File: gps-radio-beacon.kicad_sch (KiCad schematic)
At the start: 52 parts, among them J1 Conn_Coaxial, J2 Conn_01x16, J3 Conn_Coaxial, J4 Conn_01x16, J5 Conn_01x02, P1 USB_C_Plug_USB2.0, Q1 Q_PMOS_DGS, SW1 SW_Push, U1 RP2040, U2 MAX-M8Q, U3 W25Q128JVS, U4 NCP1117-3.3_SOT223, Y1 Crystal

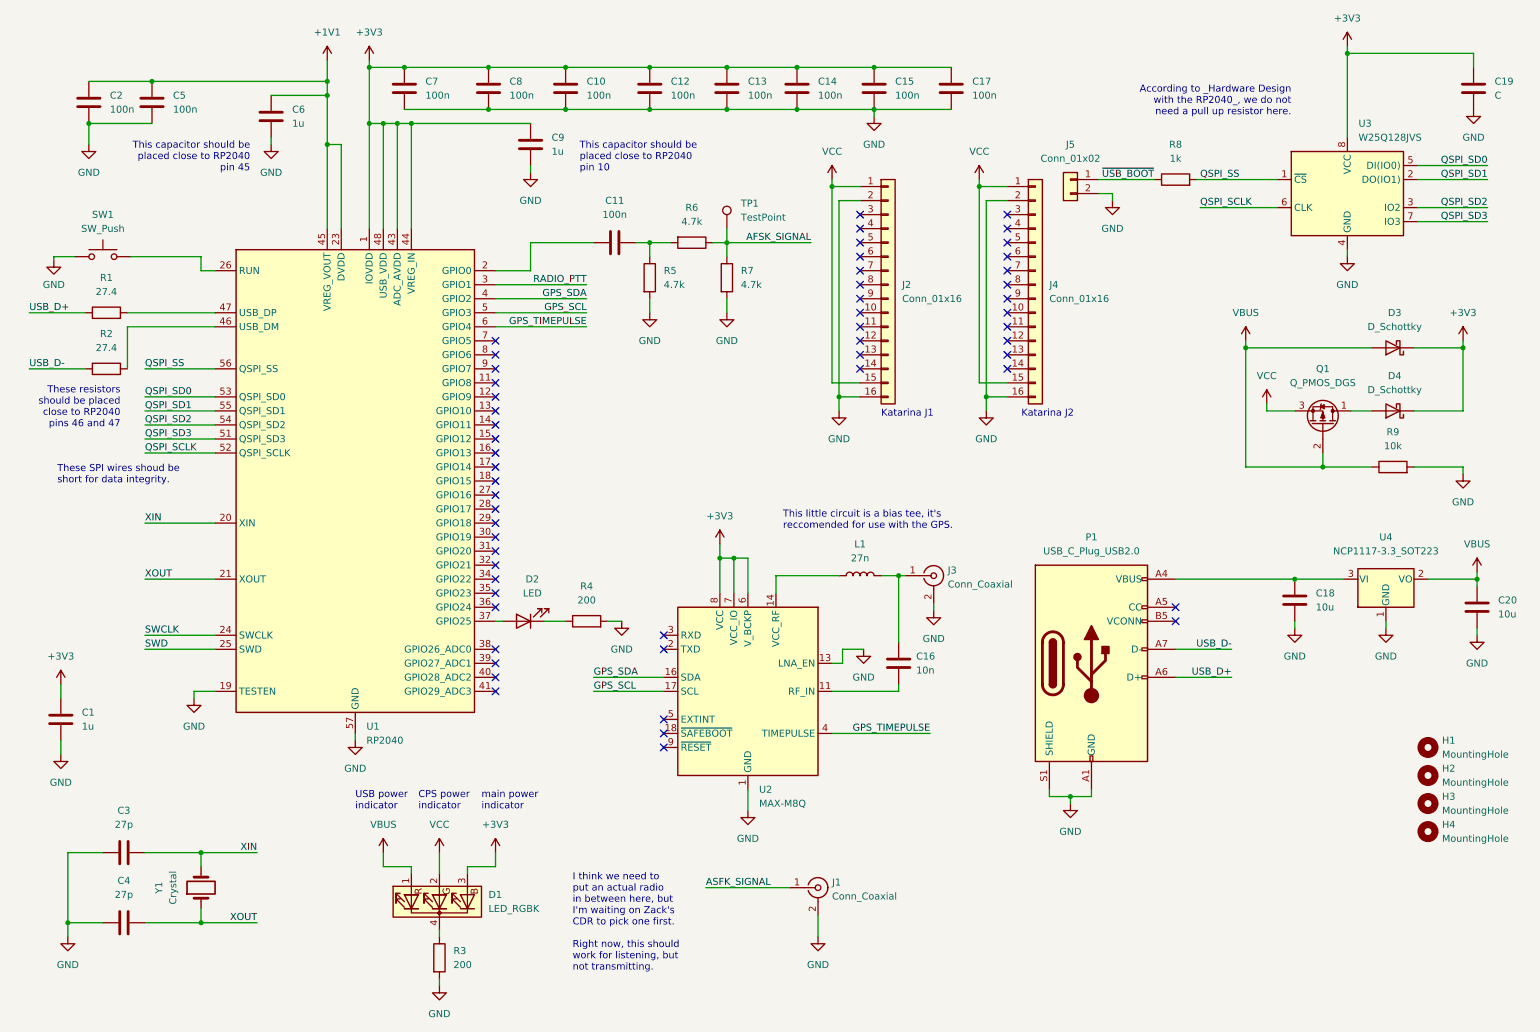
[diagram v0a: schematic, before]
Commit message: fix ERC violations
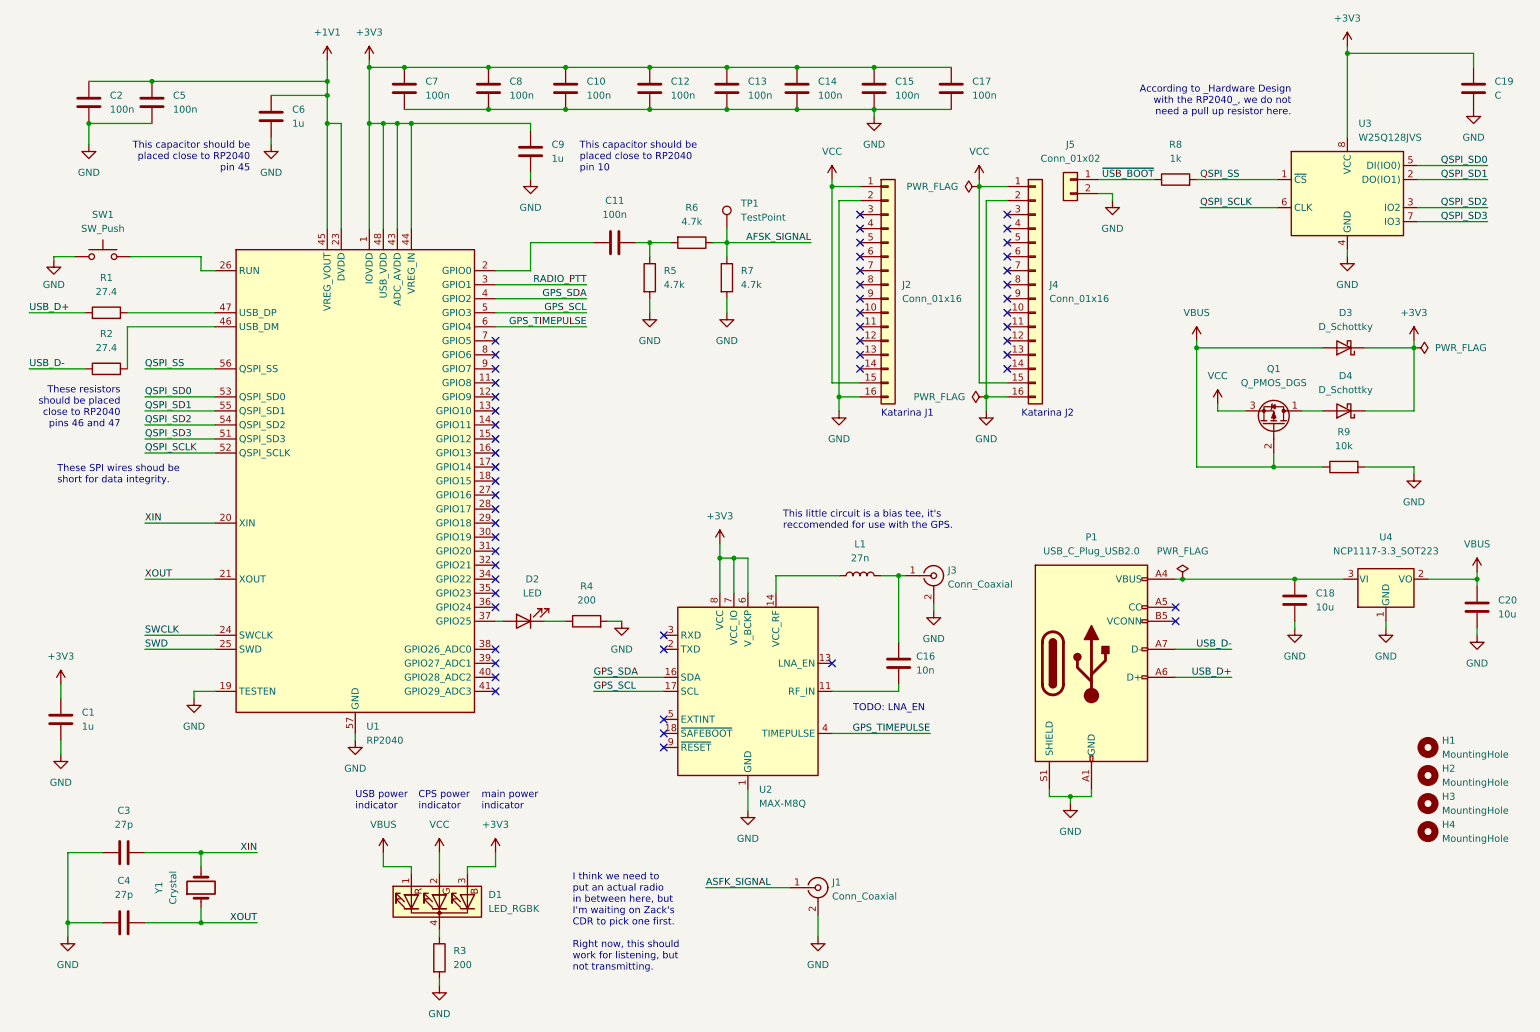
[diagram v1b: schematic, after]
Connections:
- net GND: no longer U2.13 (LNA_EN)
- no-connect marks 55 -> 56
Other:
- note added: "TODO: LNA_EN"
- moved on the sheet: C9, D3, D4, Q1, R9

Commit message: factor out power and USB to another schematic
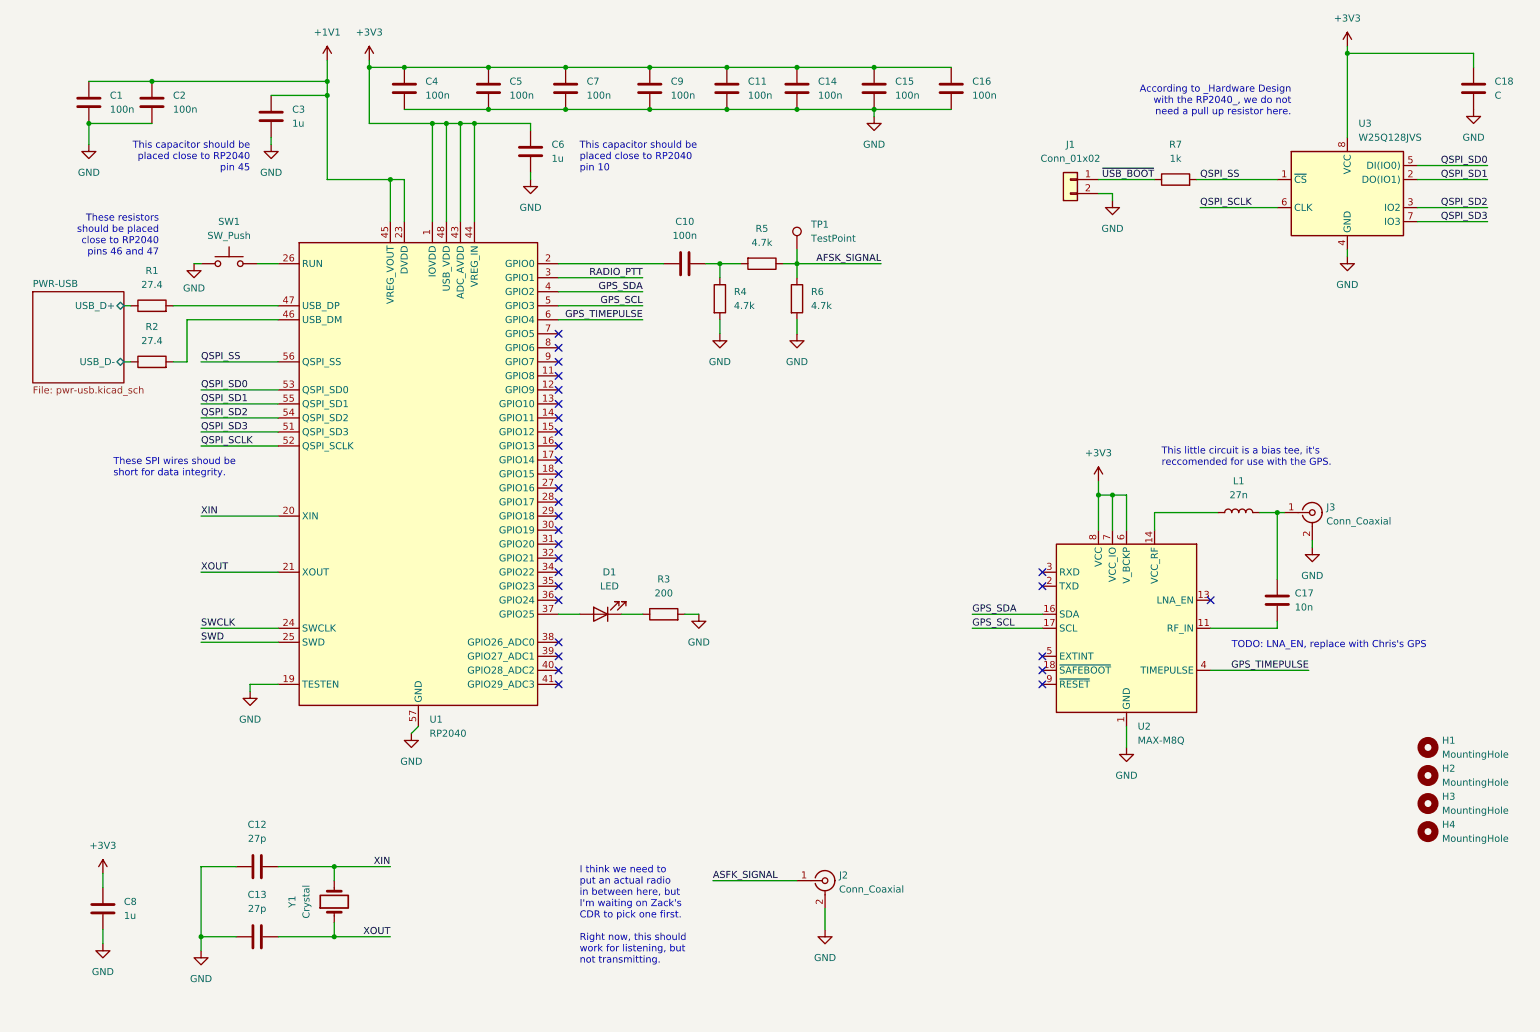
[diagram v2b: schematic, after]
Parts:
- removed C18, C20: 10u, symbol Device:C
- removed D1: LED_RGBK, symbol Device:LED_RGBK
- removed D3, D4: D_Schottky, symbol Device:D_Schottky
- removed J2, J4: Conn_01x16, symbol Connector_Generic:Conn_01x16
- removed P1: USB_C_Plug_USB2.0, symbol Connector:USB_C_Plug_USB2.0
- removed Q1: Q_PMOS_DGS, symbol Device:Q_PMOS_DGS
- removed R3: 200, symbol Device:R
- removed R9: 10k, symbol Device:R
- removed U4: NCP1117-3.3_SOT223, Package_TO_SOT_SMD:SOT-223-3_TabPin2, symbol Regulator_Linear:NCP1117-3.3_SOT223
- renumbered C2 to C1, C11 to C10, C13 to C11, C3 to C12, C4 to C13, C17 to C16, C16 to C17, C19 to C18, C5 to C2, C6 to C3, C7 to C4, C8 to C5, C9 to C6, C10 to C7, C1 to C8, C12 to C9, D2 to D1, J5 to J1, J1 to J2, R4 to R3, R5 to R4, R6 to R5, R7 to R6, R8 to R7
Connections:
- net USB_D+ renamed PWR-USB/USB_D+
- net USB_D- renamed PWR-USB/USB_D-
- no-connect marks 56 -> 30
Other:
- added sheet PWR-USB (pwr-usb.kicad_sch)
- note added: "TODO: LNA_EN, replace with Chris's GPS"
- note removed: "CPS power indicator"
- note removed: "Katarina J1"
- note removed: "Katarina J2"
- note removed: "TODO: LNA_EN"
- note removed: "USB power indicator"
- note removed: "main power indicator"
- title: GPS Radio Beacon -> GPS Radio Beacon: Power and USB
- moved on the sheet: C10, C12, C13, C17, C8, D1, J2, J3, L1, R1, R2, R3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

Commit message: refactoring, fix typos
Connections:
- net ASFK_SIGNAL is gone; now on net AFSK_SIGNAL: J2.1 (In)
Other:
- title: GPS Radio Beacon: Power and USB -> GPS Radio Beacon
- moved on the sheet: C1, C10, C11, C14, C15, C16, C2, C3, C4, C5, C6, C7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

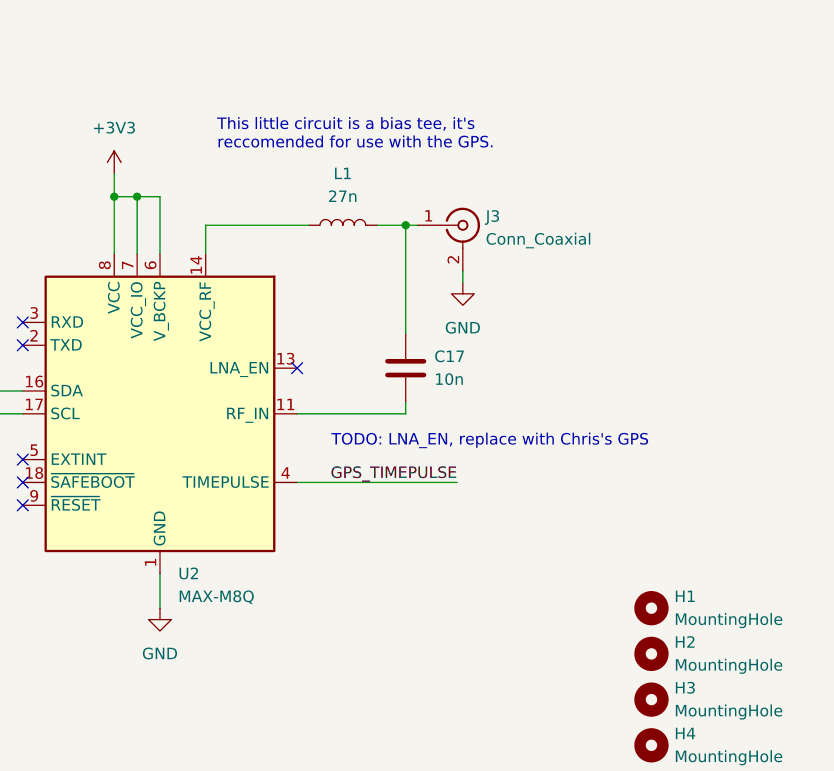
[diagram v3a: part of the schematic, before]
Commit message: migrate GPS to M10S
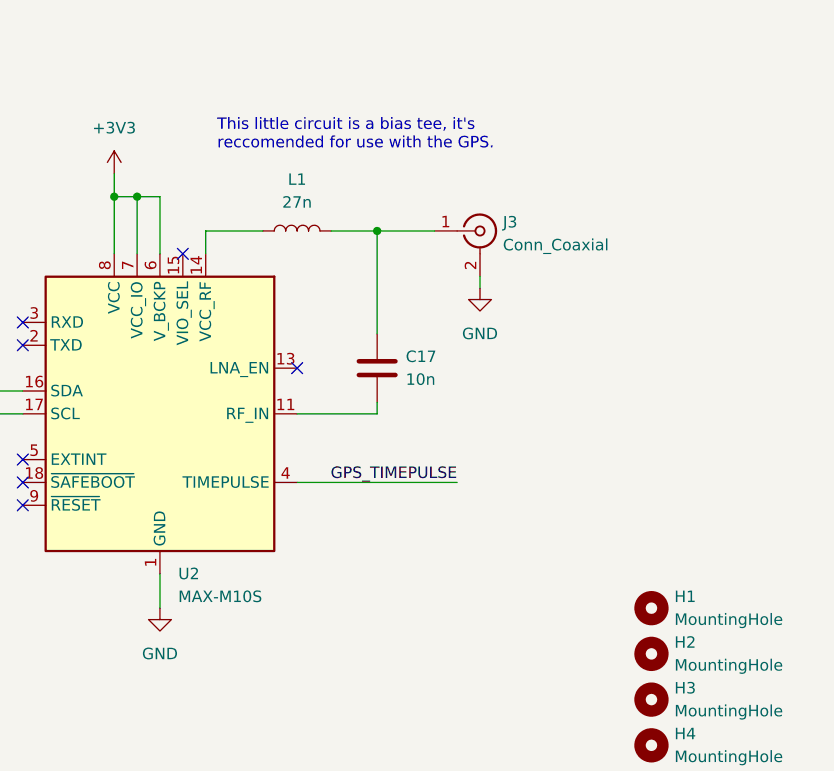
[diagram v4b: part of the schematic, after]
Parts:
- removed U2: MAX-M8Q, RF_GPS:ublox_MAX, symbol RF_GPS:MAX-M8Q
- added U2: MAX-M10S, RF_GPS:ublox_MAX, symbol GRB:MAX-M10S
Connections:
- net +3V3: now also U2.6 (V_BCKP), U2.7 (VCC_IO), U2.8 (VCC)
- net GND: now also U2.1 (GND), U2.10 (GND), U2.12 (GND)
- net GPS_SCL: now also U2.17 (SCL)
- net GPS_SDA: now also U2.16 (SDA)
- net GPS_TIMEPULSE: now also U2.4 (TIMEPULSE)
- net at C17.2: now also U2.11 (RF_IN)
- net at L1.1: now also U2.14 (VCC_RF)
- no-connect marks 30 -> 31
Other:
- note removed: "TODO: LNA_EN, replace with Chris's GPS"
- moved on the sheet: C17, J3, L1

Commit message: fix missing libraries
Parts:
- removed U2: MAX-M10S, RF_GPS:ublox_MAX, symbol GRB:MAX-M10S
- added U2: MAX-M10S, RF_GPS:ublox_MAX, symbol GRB-HW:MAX-M10S
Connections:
- net +3V3: now also U2.6 (V_BCKP), U2.7 (VCC_IO), U2.8 (VCC)
- net GND: now also U2.1 (GND), U2.10 (GND), U2.12 (GND)
- net GPS_SCL: now also U2.17 (SCL)
- net GPS_SDA: now also U2.16 (SDA)
- net GPS_TIMEPULSE: now also U2.4 (TIMEPULSE)
- net at C17.2: now also U2.11 (RF_IN)
- net at L1.1: now also U2.14 (VCC_RF)
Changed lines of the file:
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@@
     (pin "2")
-  )
-  (symbol (lib_id "GRB:MAX-M10S") (at 213.36 125.73 0) (unit 1)
-    (in_bom yes) (on_board yes) (fields_autoplaced)
-    (property "Reference" "U2" (id 0) (at 215.3794 143.51 0)
-      (effects (font (size 1.27 1.27)) (justify left))
-    )
-    (property "Value" "MAX-M10S" (id 1) (at 215.3794 146.05 0)
-      (effects (font (size 1.27 1.27)) (justify left))
-    )
-    (property "Footprint" "RF_GPS:ublox_MAX" (id 2) (at 223.52 142.24 0)
-      (effects (font (size 1.27 1.27)) hide)
-    )
-    (property "Datasheet" "https://content.u-blox.com/sites/default/files/MAX-M10S_DataSheet_UBX-20035208.pdf" (id 3) (at 213.36 125.73 0)
-      (effects (font (size 1.27 1.27)) hide)
-    )
-    (pin "1")
-    (pin "10")
-    (pin "11")
-    (pin "12")
-    (pin "13")
-    (pin "14")
-    (pin "15")
-    (pin "15")
-    (pin "16")
-    (pin "17")
-    (pin "18")
-    (pin "2")
-    (pin "3")
-    (pin "4")
-    (pin "5")
-    (pin "6")
-    (pin "7")
-    (pin "8")
-    (pin "9")
   )
   (symbol (lib_id "power:GND") (at 157.48 73.66 0) (unit 1)
@@
     (pin "2")
   )
+  (symbol (lib_id "GRB-HW:MAX-M10S") (at 213.36 125.73 0) (unit 1)
+    (in_bom yes) (on_board yes) (fields_autoplaced)
+    (property "Reference" "U2" (id 0) (at 215.3794 143.51 0)
+      (effects (font (size 1.27 1.27)) (justify left))
+    )
+    (property "Value" "MAX-M10S" (id 1) (at 215.3794 146.05 0)
+      (effects (font (size 1.27 1.27)) (justify left))
+    )
+    (property "Footprint" "RF_GPS:ublox_MAX" (id 2) (at 223.52 142.24 0)
+      (effects (font (size 1.27 1.27)) hide)
+    )
+    (property "Datasheet" "https://content.u-blox.com/sites/default/files/MAX-M10S_DataSheet_UBX-20035208.pdf" (id 3) (at 213.36 125.73 0)
+      (effects (font (size 1.27 1.27)) hide)
+    )
+    (pin "1")
+    (pin "10")
+    (pin "11")
+    (pin "12")
+    (pin "13")
+    (pin "14")
+    (pin "15")
+    (pin "15")
+    (pin "16")
+    (pin "17")
+    (pin "18")
+    (pin "2")
+    (pin "3")
+    (pin "4")
+    (pin "5")
+    (pin "6")
+    (pin "7")
+    (pin "8")
+    (pin "9")
+  )
   (symbol (lib_id "Mechanical:MountingHole") (at 267.97 147.32 0) (unit 1)
     (in_bom yes) (on_board yes) (fields_autoplaced)
@@
       (reference "U1") (unit 1) (value "RP2040") (footprint "Package_DFN_QFN:QFN-56-1EP_7x7mm_P0.4mm_EP3.2x3.2mm")
     )
-    (path "/2371c223-702e-438e-b0b6-76bc94d8fe02"
+    (path "/f66e18ab-73d7-490f-a3ef-7f27d371d061"
       (reference "U2") (unit 1) (value "MAX-M10S") (footprint "RF_GPS:ublox_MAX")
     )

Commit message: fix schematic issues
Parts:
- C18: value C -> 100n
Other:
- note added: "Reset"
- moved on the sheet: C18
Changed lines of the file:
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@@
   (junction (at 157.48 25.4) (diameter 0) (color 0 0 0 0)
+  )
+  (junction (at 185.42 33.02) (diameter 0) (color 0 0 0 0)
   )
   (junction (at 171.45 25.4) (diameter 0) (color 0 0 0 0)
@@
     (stroke (width 0) (type default) (color 0 0 0 0))
   )
+  (wire (pts (xy 185.42 33.02) (xy 185.42 34.29))
+    (stroke (width 0) (type default) (color 0 0 0 0))
+  )
   (wire (pts (xy 58.42 137.16) (xy 63.5 137.16))
     (stroke (width 0) (type default) (color 0 0 0 0))
@@
     (stroke (width 0) (type default) (color 0 0 0 0))
   )
-  (wire (pts (xy 276.225 24.13) (xy 276.225 21.59))
+  (wire (pts (xy 271.78 24.13) (xy 271.78 21.59))
     (stroke (width 0) (type default) (color 0 0 0 0))
   )
@@
     (stroke (width 0) (type default) (color 0 0 0 0))
   )
-  (wire (pts (xy 253.365 21.59) (xy 276.225 21.59))
+  (wire (pts (xy 253.365 21.59) (xy 271.78 21.59))
     (stroke (width 0) (type default) (color 0 0 0 0))
   )
@@
   )
   (wire (pts (xy 114.3 71.12) (xy 129.54 71.12))
-    (stroke (width 0) (type default) (color 0 0 0 0))
-  )
-  (wire (pts (xy 171.45 33.02) (xy 171.45 34.29))
     (stroke (width 0) (type default) (color 0 0 0 0))
   )
@@
   (text "This capacitor should be\nplaced close to RP2040\npin 10"
     (at 118.11 44.45 0)
+    (effects (font (size 1.27 1.27)) (justify left bottom))
+  )
+  (text "Reset" (at 52.07 52.07 0)
     (effects (font (size 1.27 1.27)) (justify left bottom))
   )
@@
     (pin "2")
   )
-  (symbol (lib_id "Device:C") (at 276.225 27.94 0) (unit 1)
-    (in_bom yes) (on_board yes) (fields_autoplaced)
-    (property "Reference" "C18" (id 0) (at 280.035 26.6699 0)
-      (effects (font (size 1.27 1.27)) (justify left))
-    )
-    (property "Value" "C" (id 1) (at 280.035 29.2099 0)
-      (effects (font (size 1.27 1.27)) (justify left))
-    )
-    (property "Footprint" "" (id 2) (at 277.1902 31.75 0)
-      (effects (font (size 1.27 1.27)) hide)
-    )
-    (property "Datasheet" "~" (id 3) (at 276.225 27.94 0)
+  (symbol (lib_id "Device:C") (at 271.78 27.94 0) (unit 1)
+    (in_bom yes) (on_board yes) (fields_autoplaced)
+    (property "Reference" "C18" (id 0) (at 275.59 26.6699 0)
+      (effects (font (size 1.27 1.27)) (justify left))
+    )
+    (property "Value" "100n" (id 1) (at 275.59 29.2099 0)
+      (effects (font (size 1.27 1.27)) (justify left))
+    )
+    (property "Footprint" "" (id 2) (at 272.7452 31.75 0)
+      (effects (font (size 1.27 1.27)) hide)
+    )
+    (property "Datasheet" "~" (id 3) (at 271.78 27.94 0)
       (effects (font (size 1.27 1.27)) hide)
     )
@@
     (pin "1")
   )
-  (symbol (lib_id "power:GND") (at 276.225 31.75 0) (unit 1)
-    (in_bom yes) (on_board yes) (fields_autoplaced)
-    (property "Reference" "#PWR023" (id 0) (at 276.225 38.1 0)
-      (effects (font (size 1.27 1.27)) hide)
-    )
-    (property "Value" "GND" (id 1) (at 276.225 36.83 0))
-    (property "Footprint" "" (id 2) (at 276.225 31.75 0)
-      (effects (font (size 1.27 1.27)) hide)
-    )
-    (property "Datasheet" "" (id 3) (at 276.225 31.75 0)
+  (symbol (lib_id "power:GND") (at 271.78 31.75 0) (unit 1)
+    (in_bom yes) (on_board yes) (fields_autoplaced)
+    (property "Reference" "#PWR023" (id 0) (at 271.78 38.1 0)
+      (effects (font (size 1.27 1.27)) hide)
+    )
+    (property "Value" "GND" (id 1) (at 271.78 36.83 0))
+    (property "Footprint" "" (id 2) (at 271.78 31.75 0)
+      (effects (font (size 1.27 1.27)) hide)
+    )
+    (property "Datasheet" "" (id 3) (at 271.78 31.75 0)
       (effects (font (size 1.27 1.27)) hide)
     )
@@
     (pin "2")
   )
-  (symbol (lib_id "power:GND") (at 171.45 34.29 0) (unit 1)
-    (in_bom yes) (on_board yes) (fields_autoplaced)
-    (property "Reference" "#PWR015" (id 0) (at 171.45 40.64 0)
-      (effects (font (size 1.27 1.27)) hide)
-    )
-    (property "Value" "GND" (id 1) (at 171.45 39.37 0))
-    (property "Footprint" "" (id 2) (at 171.45 34.29 0)
-      (effects (font (size 1.27 1.27)) hide)
-    )
-    (property "Datasheet" "" (id 3) (at 171.45 34.29 0)
+  (symbol (lib_id "power:GND") (at 185.42 34.29 0) (unit 1)
+    (in_bom yes) (on_board yes) (fields_autoplaced)
+    (property "Reference" "#PWR015" (id 0) (at 185.42 40.64 0)
+      (effects (font (size 1.27 1.27)) hide)
+    )
+    (property "Value" "GND" (id 1) (at 185.42 39.37 0))
+    (property "Footprint" "" (id 2) (at 185.42 34.29 0)
+      (effects (font (size 1.27 1.27)) hide)
+    )
+    (property "Datasheet" "" (id 3) (at 185.42 34.29 0)
       (effects (font (size 1.27 1.27)) hide)
     )
@@
     )
     (path "/111e122d-9736-42dc-96fa-f4fc98b30c52"
-      (reference "C18") (unit 1) (value "C") (footprint "")
+      (reference "C18") (unit 1) (value "100n") (footprint "")
     )
     (path "/347cbce7-1bff-4e1d-98eb-b36eb30fbe98/4e4ef739-b653-47f4-8f5f-f80bd773cafa"
